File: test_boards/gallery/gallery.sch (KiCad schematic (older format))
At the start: 19 parts

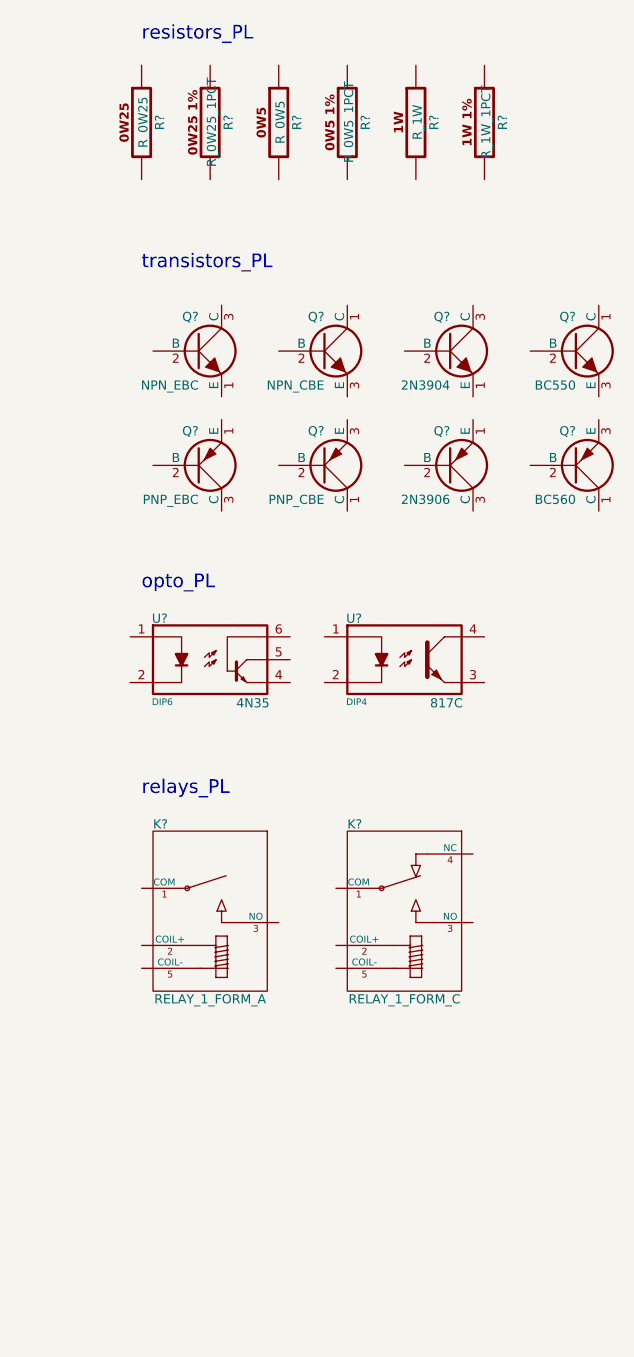
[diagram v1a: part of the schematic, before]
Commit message: tweaking relays, adding dc barrel jacks
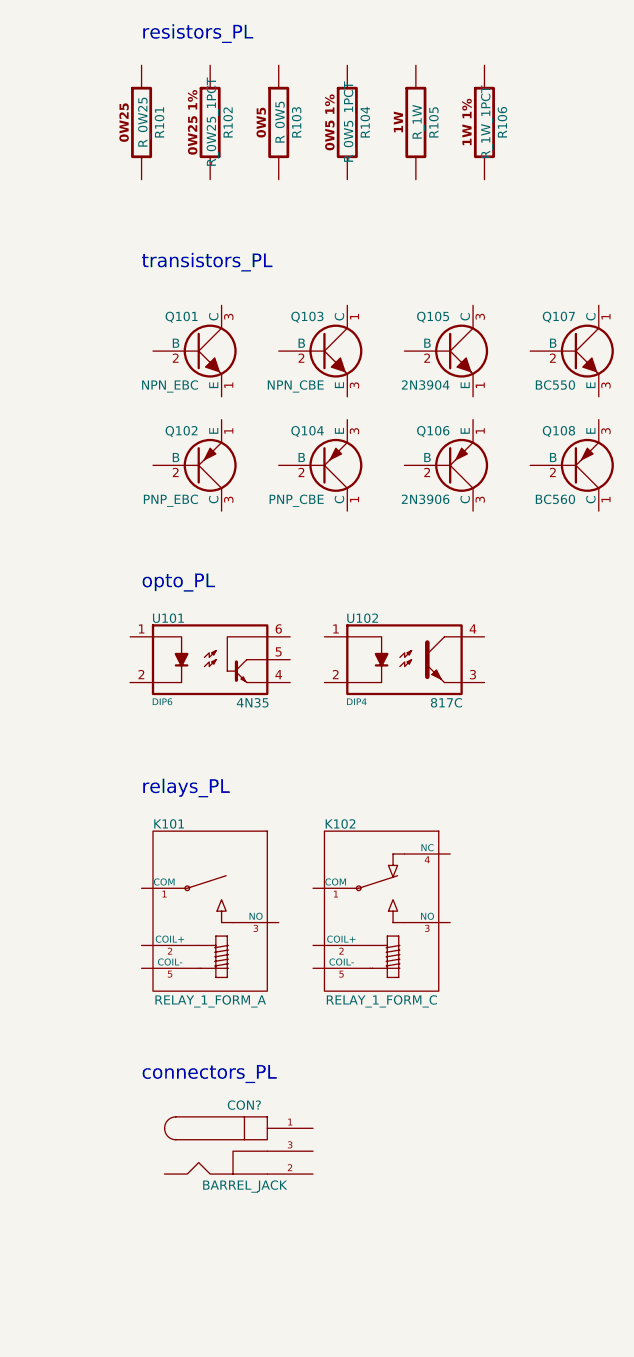
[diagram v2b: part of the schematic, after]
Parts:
- removed K?: RELAY_1_FORM_A, ~, symbol RELAY_1_FORM_A
- removed K?: RELAY_1_FORM_C, ~, symbol RELAY_1_FORM_C
- added CON?: BARREL_JACK, ~, symbol BARREL_JACK
- added K101: RELAY_1_FORM_A, ~, symbol RELAY_1_FORM_A
- added K102: RELAY_1_FORM_C, ~, symbol RELAY_1_FORM_C
- gave numbers to parts that had none: 17
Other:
- note added: "connectors_PL"
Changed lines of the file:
@@
 EESchema Schematic File Version 2
+LIBS:connectors_PL
 LIBS:transistors_PL
 LIBS:mounting_holes_PL
@@
 Sheet 1 1
 Title ""
-Date "15 mar 2014"
+Date "17 mar 2014"
 Rev ""
 Comp ""
@@
 $EndDescr
 $Comp
-L R_0W25 R?
+L R_0W25 R101
 U 1 1 5323CBE8
 P 700 1050
-F 0 "R?" V 780 1050 40  0000 C CNN
+F 0 "R101" V 780 1050 40  0000 C CNN
 F 1 "R_0W25" V 707 1051 40  0000 C CNN
 F 2 "~" V 630 1050 30  0000 C CNN
@@
 $EndComp
 $Comp
-L R_0W25_1PCT R?
+L R_0W25_1PCT R102
 U 1 1 5323CBF9
 P 1000 1050
-F 0 "R?" V 1080 1050 40  0000 C CNN
+F 0 "R102" V 1080 1050 40  0000 C CNN
 F 1 "R_0W25_1PCT" V 1007 1051 40  0000 C CNN
 F 2 "~" V 930 1050 30  0000 C CNN
@@
 $EndComp
 $Comp
-L R_0W5 R?
+L R_0W5 R103
 U 1 1 5323CC08
 P 1300 1050
-F 0 "R?" V 1380 1050 40  0000 C CNN
+F 0 "R103" V 1380 1050 40  0000 C CNN
 F 1 "R_0W5" V 1307 1051 40  0000 C CNN
 F 2 "~" V 1230 1050 30  0000 C CNN
@@
 $EndComp
 $Comp
-L R_0W5_1PCT R?
+L R_0W5_1PCT R104
 U 1 1 5323CC21
 P 1600 1050
-F 0 "R?" V 1680 1050 40  0000 C CNN
+F 0 "R104" V 1680 1050 40  0000 C CNN
 F 1 "R_0W5_1PCT" V 1607 1051 40  0000 C CNN
 F 2 "~" V 1530 1050 30  0000 C CNN
@@
 $EndComp
 $Comp
-L R_1W R?
+L R_1W R105
 U 1 1 5323CC30
 P 1900 1050
-F 0 "R?" V 1980 1050 40  0000 C CNN
+F 0 "R105" V 1980 1050 40  0000 C CNN
 F 1 "R_1W" V 1907 1051 40  0000 C CNN
 F 2 "~" V 1830 1050 30  0000 C CNN
@@
 $EndComp
 $Comp
-L R_1W_1PCT R?
+L R_1W_1PCT R106
 U 1 1 5323CC3F
 P 2200 1050
-F 0 "R?" V 2280 1050 40  0000 C CNN
+F 0 "R106" V 2280 1050 40  0000 C CNN
 F 1 "R_1W_1PCT" V 2207 1051 40  0000 C CNN
 F 2 "~" V 2130 1050 30  0000 C CNN
@@
 transistors_PL
 $Comp
-L 4N35 U?
+L 4N35 U101
 U 1 1 5323CCFD
 P 1000 3400
-F 0 "U?" H 745 3580 40  0000 L CNN
+F 0 "U101" H 745 3580 40  0000 L CNN
 F 1 "4N35" H 1260 3210 40  0000 R CNN
 F 2 "DIP6" H 745 3215 29  0000 L CNN
@@
 opto_PL
 $Comp
-L 817C U?
+L 817C U102
 U 1 1 5323CD26
 P 1850 3400
-F 0 "U?" H 1595 3580 40  0000 L CNN
+F 0 "U102" H 1595 3580 40  0000 L CNN
 F 1 "817C" H 2105 3210 40  0000 R CNN
 F 2 "DIP4" H 1595 3215 29  0000 L CNN
@@
 	1    0    0    -1
 $EndComp
-$Comp
-L RELAY_1_FORM_A K?
-U 1 1 5323CD50
-P 1000 4500
-F 0 "K?" H 750 4880 40  0000 L CNN
-F 1 "RELAY_1_FORM_A" H 1000 4115 40  0000 C CNN
-F 2 "~" H 995 4680 60  0000 C CNN
-F 3 "~" H 995 4680 60  0000 C CNN
-	1    1000 4500
-	1    0    0    -1
-$EndComp
-$Comp
-L RELAY_1_FORM_C K?
-U 1 1 5323CD5F
-P 1850 4500
-F 0 "K?" H 1600 4880 40  0000 L CNN
-F 1 "RELAY_1_FORM_C" H 1850 4115 40  0000 C CNN
-F 2 "~" H 1845 4680 60  0000 C CNN
-F 3 "~" H 1845 4680 60  0000 C CNN
-	1    1850 4500
-	1    0    0    -1
-$EndComp
 Text Notes 700  4000 0    60   ~ 0
 relays_PL
 $Comp
-L NPN_EBC Q?
+L NPN_EBC Q101
 U 1 1 5323DE26
 P 950 2050
-F 0 "Q?" H 950 2200 40  0000 R CNN
+F 0 "Q101" H 950 2200 40  0000 R CNN
 F 1 "NPN_EBC" H 950 1900 40  0000 R CNN
 F 2 "~" H 950 2050 60  0000 C CNN
@@
 $EndComp
 $Comp
-L PNP_EBC Q?
+L PNP_EBC Q102
 U 1 1 5323DE35
 P 950 2550
-F 0 "Q?" H 950 2700 40  0000 R CNN
+F 0 "Q102" H 950 2700 40  0000 R CNN
 F 1 "PNP_EBC" H 950 2400 40  0000 R CNN
 F 2 "~" H 950 2550 60  0000 C CNN
@@
 $EndComp
 $Comp
-L NPN_CBE Q?
+L NPN_CBE Q103
 U 1 1 5323DE44
 P 1500 2050
-F 0 "Q?" H 1500 2200 40  0000 R CNN
+F 0 "Q103" H 1500 2200 40  0000 R CNN
 F 1 "NPN_CBE" H 1500 1900 40  0000 R CNN
 F 2 "~" H 1500 2050 60  0000 C CNN
@@
 $EndComp
 $Comp
-L PNP_CBE Q?
+L PNP_CBE Q104
 U 1 1 5323DE53
 P 1500 2550
-F 0 "Q?" H 1500 2700 40  0000 R CNN
+F 0 "Q104" H 1500 2700 40  0000 R CNN
 F 1 "PNP_CBE" H 1500 2400 40  0000 R CNN
 F 2 "~" H 1500 2550 60  0000 C CNN
@@
 $EndComp
 $Comp
-L 2N3904 Q?
+L 2N3904 Q105
 U 1 1 5323DE62
 P 2050 2050
-F 0 "Q?" H 2050 2200 40  0000 R CNN
+F 0 "Q105" H 2050 2200 40  0000 R CNN
 F 1 "2N3904" H 2050 1900 40  0000 R CNN
 F 2 "~" H 2050 2050 60  0000 C CNN
@@
 $EndComp
 $Comp
-L 2N3906 Q?
+L 2N3906 Q106
 U 1 1 5323DE71
 P 2050 2550
-F 0 "Q?" H 2050 2700 40  0000 R CNN
+F 0 "Q106" H 2050 2700 40  0000 R CNN
 F 1 "2N3906" H 2050 2400 40  0000 R CNN
 F 2 "~" H 2050 2550 60  0000 C CNN
@@
 $EndComp
 $Comp
-L BC550 Q?
+L BC550 Q107
 U 1 1 5323DE80
 P 2600 2050
-F 0 "Q?" H 2600 2200 40  0000 R CNN
+F 0 "Q107" H 2600 2200 40  0000 R CNN
 F 1 "BC550" H 2600 1900 40  0000 R CNN
 F 2 "~" H 2600 2050 60  0000 C CNN
@@
 $EndComp
 $Comp
-L BC560 Q?
+L BC560 Q108
 U 1 1 5323DE8F
 P 2600 2550
-F 0 "Q?" H 2600 2700 40  0000 R CNN
+F 0 "Q108" H 2600 2700 40  0000 R CNN
 F 1 "BC560" H 2600 2400 40  0000 R CNN
 F 2 "~" H 2600 2550 60  0000 C CNN
@@
 $EndComp
 $Comp
-L HOLE H?
+L HOLE H101
 U 1 1 5323DFF1
 P 750 7550
-F 0 "H?" H 750 7605 40  0000 C CNN
+F 0 "H101" H 750 7605 40  0000 C CNN
 F 1 "HOLE" H 750 7490 30  0000 C CNN
 F 2 "~" H 750 7550 60  0000 C CNN
@@
 Text Notes 700  7350 0    60   ~ 0
 mounting_holes_PL
+Text Notes 700  5250 0    60   ~ 0
+connectors_PL
+$Comp
+L RELAY_1_FORM_A K101
+U 1 1 53265C18
+P 1000 4500
+F 0 "K101" H 750 4880 40  0000 L CNN
+F 1 "RELAY_1_FORM_A" H 1000 4110 40  0000 C CNN
+F 2 "~" H 995 4680 60  0000 C CNN
+F 3 "~" H 995 4680 60  0000 C CNN
+	1    1000 4500
+	1    0    0    -1
+$EndComp
+$Comp
+L RELAY_1_FORM_C K102
+U 1 1 53265C27
+P 1750 4500
+F 0 "K102" H 1500 4880 40  0000 L CNN
+F 1 "RELAY_1_FORM_C" H 1750 4110 40  0000 C CNN
+F 2 "~" H 1745 4680 60  0000 C CNN
+F 3 "~" H 1745 4680 60  0000 C CNN
+	1    1750 4500
+	1    0    0    -1
+$EndComp
+$Comp
+L BARREL_JACK CON?
+U 1 1 53265E33
+P 1150 5550
+F 0 "CON?" H 1150 5750 40  0000 C CNN
+F 1 "BARREL_JACK" H 1150 5400 40  0000 C CNN
+F 2 "~" H 1150 5550 60  0000 C CNN
+F 3 "~" H 1150 5550 60  0000 C CNN
+	1    1150 5550
+	1    0    0    -1
+$EndComp
 $EndSCHEMATC

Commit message: adding regulators and displays
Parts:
- added DS?: AMMETER_H, ~, symbol AMMETER_H
- added DS?: AMMETER_V, ~, symbol AMMETER_V
- added DS?: VOLTMETER, ~, symbol VOLTMETER
- added U?: 7805, ~, symbol 7805
- added U?: 78L05, ~, symbol 78L05
- added U?: LM317, ~, symbol LM317
- added U?: LM337, ~, symbol LM337
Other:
- note added: "displays_PL"
- note added: "regulators_PL"
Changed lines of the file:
@@
 EESchema Schematic File Version 2
+LIBS:displays_PL
+LIBS:regulators_PL
 LIBS:connectors_PL
 LIBS:transistors_PL
@@
 Sheet 1 1
 Title ""
-Date "17 mar 2014"
+Date "20 mar 2014"
 Rev ""
 Comp ""
@@
 	1    0    0    -1
 $EndComp
+$Comp
+L AMMETER_H DS?
+U 1 1 532A694E
+P 1700 5500
+F 0 "DS?" H 1750 5650 40  0000 L CNN
+F 1 "AMMETER_H" H 2550 5100 40  0000 R CNN
+F 2 "~" H 2530 5900 60  0000 C CNN
+F 3 "~" H 2530 5900 60  0000 C CNN
+	1    1700 5500
+	1    0    0    -1
+$EndComp
+$Comp
+L AMMETER_V DS?
+U 1 1 532A695D
+P 2850 5500
+F 0 "DS?" H 2900 5650 40  0000 L CNN
+F 1 "AMMETER_V" H 3700 5100 40  0000 R CNN
+F 2 "~" H 3680 5900 60  0000 C CNN
+F 3 "~" H 3680 5900 60  0000 C CNN
+	1    2850 5500
+	1    0    0    -1
+$EndComp
+$Comp
+L VOLTMETER DS?
+U 1 1 532A696C
+P 4000 5500
+F 0 "DS?" H 4050 5650 40  0000 L CNN
+F 1 "VOLTMETER" H 4850 5100 40  0000 R CNN
+F 2 "~" H 4830 5900 60  0000 C CNN
+F 3 "~" H 4830 5900 60  0000 C CNN
+	1    4000 5500
+	1    0    0    -1
+$EndComp
+Text Notes 1650 5250 0    60   ~ 0
+displays_PL
+$Comp
+L 7805 U?
+U 1 1 532A6997
+P 1050 6500
+F 0 "U?" H 850 6660 40  0000 L BNN
+F 1 "7805" H 1250 6330 40  0000 R TNN
+F 2 "~" H 1050 6500 60  0000 C CNN
+F 3 "~" H 1050 6500 60  0000 C CNN
+	1    1050 6500
+	1    0    0    -1
+$EndComp
+$Comp
+L 78L05 U?
+U 1 1 532A69B5
+P 1800 6500
+F 0 "U?" H 1600 6660 40  0000 L BNN
+F 1 "78L05" H 2000 6330 40  0000 R TNN
+F 2 "~" H 1800 6500 60  0000 C CNN
+F 3 "~" H 1800 6500 60  0000 C CNN
+	1    1800 6500
+	1    0    0    -1
+$EndComp
+$Comp
+L LM317 U?
+U 1 1 532A69C4
+P 2550 6500
+F 0 "U?" H 2350 6660 40  0000 L BNN
+F 1 "LM317" H 2750 6330 40  0000 R TNN
+F 2 "~" H 2550 6500 60  0000 C CNN
+F 3 "~" H 2550 6500 60  0000 C CNN
+	1    2550 6500
+	1    0    0    -1
+$EndComp
+$Comp
+L LM337 U?
+U 1 1 532A69D3
+P 3300 6500
+F 0 "U?" H 3100 6660 40  0000 L BNN
+F 1 "LM337" H 3500 6330 40  0000 R TNN
+F 2 "~" H 3300 6500 60  0000 C CNN
+F 3 "~" H 3300 6500 60  0000 C CNN
+	1    3300 6500
+	1    0    0    -1
+$EndComp
+Text Notes 750  6250 0    60   ~ 0
+regulators_PL
 $EndSCHEMATC

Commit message: updating gallery schematic
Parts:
- added C?: C_CER, ~, symbol C_CER
- added C?: C_EL, ~, symbol C_EL
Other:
- note added: "capacitors_PL"
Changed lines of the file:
@@
 EESchema Schematic File Version 2
+LIBS:capacitors_PL
 LIBS:displays_PL
 LIBS:regulators_PL
@@
 Sheet 1 1
 Title ""
-Date "20 mar 2014"
+Date "23 mar 2014"
 Rev ""
 Comp ""
@@
 Text Notes 750  6250 0    60   ~ 0
 regulators_PL
+Text Notes 2900 700  0    60   ~ 0
+capacitors_PL
+$Comp
+L C_CER C?
+U 1 1 532F0423
+P 3000 1000
+F 0 "C?" H 3020 1060 30  0000 L BNN
+F 1 "C_CER" H 3020 940 30  0000 L TNN
+F 2 "~" H 3038 850 30  0000 C CNN
+F 3 "~" H 3000 1000 60  0000 C CNN
+	1    3000 1000
+	1    0    0    -1
+$EndComp
+$Comp
+L C_EL C?
+U 1 1 532F0432
+P 3350 1000
+F 0 "C?" H 3370 1060 30  0000 L BNN
+F 1 "C_EL" H 3370 910 30  0000 L TNN
+F 2 "~" H 3388 850 30  0000 C CNN
+F 3 "~" H 3350 1000 60  0000 C CNN
+	1    3350 1000
+	1    0    0    -1
+$EndComp
 $EndSCHEMATC

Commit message: tweaking caps
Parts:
- gave numbers to parts that had none: 10
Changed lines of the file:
@@
 $EndComp
 $Comp
-L BARREL_JACK CON?
+L BARREL_JACK CON101
 U 1 1 53265E33
 P 1150 5550
-F 0 "CON?" H 1150 5750 40  0000 C CNN
+F 0 "CON101" H 1150 5750 40  0000 C CNN
 F 1 "BARREL_JACK" H 1150 5400 40  0000 C CNN
 F 2 "~" H 1150 5550 60  0000 C CNN
@@
 $EndComp
 $Comp
-L AMMETER_H DS?
+L AMMETER_H DS101
 U 1 1 532A694E
 P 1700 5500
-F 0 "DS?" H 1750 5650 40  0000 L CNN
+F 0 "DS101" H 1750 5650 40  0000 L CNN
 F 1 "AMMETER_H" H 2550 5100 40  0000 R CNN
 F 2 "~" H 2530 5900 60  0000 C CNN
@@
 $EndComp
 $Comp
-L AMMETER_V DS?
+L AMMETER_V DS102
 U 1 1 532A695D
 P 2850 5500
-F 0 "DS?" H 2900 5650 40  0000 L CNN
+F 0 "DS102" H 2900 5650 40  0000 L CNN
 F 1 "AMMETER_V" H 3700 5100 40  0000 R CNN
 F 2 "~" H 3680 5900 60  0000 C CNN
@@
 $EndComp
 $Comp
-L VOLTMETER DS?
+L VOLTMETER DS103
 U 1 1 532A696C
 P 4000 5500
-F 0 "DS?" H 4050 5650 40  0000 L CNN
+F 0 "DS103" H 4050 5650 40  0000 L CNN
 F 1 "VOLTMETER" H 4850 5100 40  0000 R CNN
 F 2 "~" H 4830 5900 60  0000 C CNN
@@
 displays_PL
 $Comp
-L 7805 U?
+L 7805 U103
 U 1 1 532A6997
 P 1050 6500
-F 0 "U?" H 850 6660 40  0000 L BNN
+F 0 "U103" H 850 6660 40  0000 L BNN
 F 1 "7805" H 1250 6330 40  0000 R TNN
 F 2 "~" H 1050 6500 60  0000 C CNN
@@
 $EndComp
 $Comp
-L 78L05 U?
+L 78L05 U104
 U 1 1 532A69B5
 P 1800 6500
-F 0 "U?" H 1600 6660 40  0000 L BNN
+F 0 "U104" H 1600 6660 40  0000 L BNN
 F 1 "78L05" H 2000 6330 40  0000 R TNN
 F 2 "~" H 1800 6500 60  0000 C CNN
@@
 $EndComp
 $Comp
-L LM317 U?
+L LM317 U105
 U 1 1 532A69C4
 P 2550 6500
-F 0 "U?" H 2350 6660 40  0000 L BNN
+F 0 "U105" H 2350 6660 40  0000 L BNN
 F 1 "LM317" H 2750 6330 40  0000 R TNN
 F 2 "~" H 2550 6500 60  0000 C CNN
@@
 $EndComp
 $Comp
-L LM337 U?
+L LM337 U106
 U 1 1 532A69D3
 P 3300 6500
-F 0 "U?" H 3100 6660 40  0000 L BNN
+F 0 "U106" H 3100 6660 40  0000 L BNN
 F 1 "LM337" H 3500 6330 40  0000 R TNN
 F 2 "~" H 3300 6500 60  0000 C CNN
@@
 capacitors_PL
 $Comp
-L C_CER C?
+L C_CER C101
 U 1 1 532F0423
 P 3000 1000
-F 0 "C?" H 3020 1060 30  0000 L BNN
+F 0 "C101" H 3020 1060 30  0000 L BNN
 F 1 "C_CER" H 3020 940 30  0000 L TNN
 F 2 "~" H 3038 850 30  0000 C CNN
@@
 $EndComp
 $Comp
-L C_EL C?
+L C_EL C102
 U 1 1 532F0432
 P 3350 1000
-F 0 "C?" H 3370 1060 30  0000 L BNN
+F 0 "C102" H 3370 1060 30  0000 L BNN
 F 1 "C_EL" H 3370 910 30  0000 L TNN
 F 2 "~" H 3388 850 30  0000 C CNN

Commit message: adding mini toggle switch
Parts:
- added SW?: SPDT, ~, symbol SPDT
- added SW?: SP6T, ~, symbol SP6T
- added SW?: DP6T, ~, symbol DP6T
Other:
- note added: "switches_PL"
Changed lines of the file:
@@
 EESchema Schematic File Version 2
+LIBS:switches_PL
 LIBS:capacitors_PL
 LIBS:displays_PL
@@
 	1    0    0    -1
 $EndComp
+$Comp
+L SPDT SW?
+U 1 1 532F106F
+P 2500 4300
+F 0 "SW?" H 2720 4400 40  0000 C CNN
+F 1 "SPDT" H 2780 4230 40  0000 C CNN
+F 2 "~" H 2880 4300 60  0000 C CNN
+F 3 "~" H 2880 4300 60  0000 C CNN
+	1    2500 4300
+	1    0    0    -1
+$EndComp
+Text Notes 2450 4000 0    60   ~ 0
+switches_PL
+$Comp
+L SP6T SW?
+U 1 1 532F108A
+P 3600 4500
+F 0 "SW?" H 3900 4550 40  0000 C CNN
+F 1 "SP6T" H 3900 4450 40  0000 C CNN
+F 2 "~" H 3600 5500 60  0000 C CNN
+F 3 "~" H 3600 5500 60  0000 C CNN
+	1    3600 4500
+	1    0    0    -1
+$EndComp
+$Comp
+L DP6T SW?
+U 1 1 532F1099
+P 5400 4500
+F 0 "SW?" H 5700 4550 40  0000 C CNN
+F 1 "DP6T" H 5700 4450 40  0000 C CNN
+F 2 "~" H 5400 5500 60  0000 C CNN
+F 3 "~" H 5400 5500 60  0000 C CNN
+	1    5400 4500
+	1    0    0    -1
+$EndComp

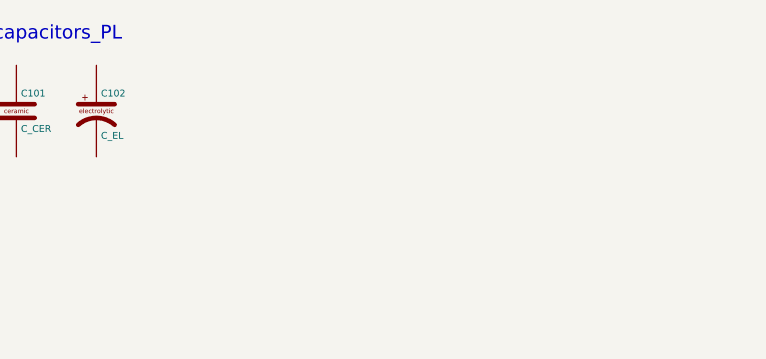
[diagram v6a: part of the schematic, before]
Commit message: adding diodes
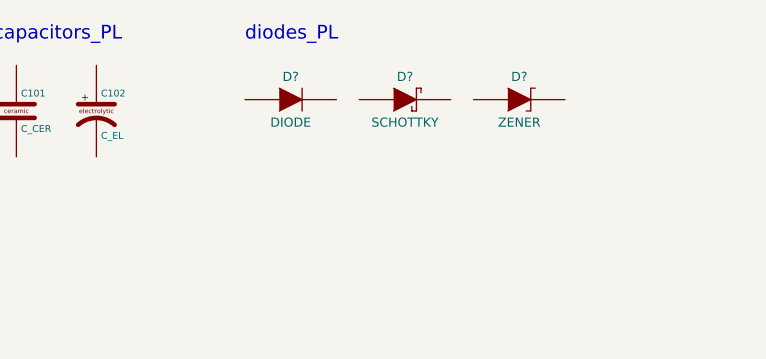
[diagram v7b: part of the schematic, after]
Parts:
- added D?: DIODE, ~, symbol DIODE
- added D?: SCHOTTKY, ~, symbol SCHOTTKY
- added D?: ZENER, ~, symbol ZENER
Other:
- note added: "diodes_PL"
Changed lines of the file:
@@
 EESchema Schematic File Version 2
+LIBS:diodes_PL
 LIBS:switches_PL
 LIBS:capacitors_PL
@@
 	1    0    0    -1
 $EndComp
+Text Notes 4000 700  0    60   ~ 0
+diodes_PL
+$Comp
+L DIODE D?
+U 1 1 532F4AEC
+P 4200 950
+F 0 "D?" H 4200 1050 40  0000 C CNN
+F 1 "DIODE" H 4200 850 40  0000 C CNN
+F 2 "~" H 4200 950 60  0000 C CNN
+F 3 "~" H 4200 950 60  0000 C CNN
+	1    4200 950
+	1    0    0    -1
+$EndComp
+$Comp
+L SCHOTTKY D?
+U 1 1 532F4AFB
+P 4700 950
+F 0 "D?" H 4700 1050 40  0000 C CNN
+F 1 "SCHOTTKY" H 4700 850 40  0000 C CNN
+F 2 "~" H 4700 950 60  0000 C CNN
+F 3 "~" H 4700 950 60  0000 C CNN
+	1    4700 950
+	1    0    0    -1
+$EndComp
+$Comp
+L ZENER D?
+U 1 1 532F4B0A
+P 5200 950
+F 0 "D?" H 5200 1050 40  0000 C CNN
+F 1 "ZENER" H 5200 850 40  0000 C CNN
+F 2 "~" H 5200 950 60  0000 C CNN
+F 3 "~" H 5200 950 60  0000 C CNN
+	1    5200 950
+	1    0    0    -1
+$EndComp

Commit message: adding potentiometer symbols
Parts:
- added RV?: POT, ~, symbol POT
- added RV?: POT_10T, ~, symbol POT_10T
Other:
- moved on the sheet: C101, C102, D?
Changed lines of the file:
@@
 Text Notes 750  6250 0    60   ~ 0
 regulators_PL
-Text Notes 2900 700  0    60   ~ 0
+Text Notes 3850 700  0    60   ~ 0
 capacitors_PL
 $Comp
 L C_CER C101
 U 1 1 532F0423
-P 3000 1000
-F 0 "C101" H 3020 1060 30  0000 L BNN
-F 1 "C_CER" H 3020 940 30  0000 L TNN
-F 2 "~" H 3038 850 30  0000 C CNN
-F 3 "~" H 3000 1000 60  0000 C CNN
-	1    3000 1000
+P 3950 1000
+F 0 "C101" H 3970 1060 30  0000 L BNN
+F 1 "C_CER" H 3970 940 30  0000 L TNN
+F 2 "~" H 3988 850 30  0000 C CNN
+F 3 "~" H 3950 1000 60  0000 C CNN
+	1    3950 1000
 	1    0    0    -1
 $EndComp
@@
 L C_EL C102
 U 1 1 532F0432
-P 3350 1000
-F 0 "C102" H 3370 1060 30  0000 L BNN
-F 1 "C_EL" H 3370 910 30  0000 L TNN
-F 2 "~" H 3388 850 30  0000 C CNN
-F 3 "~" H 3350 1000 60  0000 C CNN
-	1    3350 1000
+P 4300 1000
+F 0 "C102" H 4320 1060 30  0000 L BNN
+F 1 "C_EL" H 4320 910 30  0000 L TNN
+F 2 "~" H 4338 850 30  0000 C CNN
+F 3 "~" H 4300 1000 60  0000 C CNN
+	1    4300 1000
 	1    0    0    -1
 $EndComp
@@
 	1    0    0    -1
 $EndComp
-Text Notes 4000 700  0    60   ~ 0
+Text Notes 4950 700  0    60   ~ 0
 diodes_PL
 $Comp
 L DIODE D?
 U 1 1 532F4AEC
-P 4200 950
-F 0 "D?" H 4200 1050 40  0000 C CNN
-F 1 "DIODE" H 4200 850 40  0000 C CNN
-F 2 "~" H 4200 950 60  0000 C CNN
-F 3 "~" H 4200 950 60  0000 C CNN
-	1    4200 950
+P 5150 950
+F 0 "D?" H 5150 1050 40  0000 C CNN
+F 1 "DIODE" H 5150 850 40  0000 C CNN
+F 2 "~" H 5150 950 60  0000 C CNN
+F 3 "~" H 5150 950 60  0000 C CNN
+	1    5150 950
 	1    0    0    -1
 $EndComp
@@
 L SCHOTTKY D?
 U 1 1 532F4AFB
-P 4700 950
-F 0 "D?" H 4700 1050 40  0000 C CNN
-F 1 "SCHOTTKY" H 4700 850 40  0000 C CNN
-F 2 "~" H 4700 950 60  0000 C CNN
-F 3 "~" H 4700 950 60  0000 C CNN
-	1    4700 950
+P 5650 950
+F 0 "D?" H 5650 1050 40  0000 C CNN
+F 1 "SCHOTTKY" H 5650 850 40  0000 C CNN
+F 2 "~" H 5650 950 60  0000 C CNN
+F 3 "~" H 5650 950 60  0000 C CNN
+	1    5650 950
 	1    0    0    -1
 $EndComp
@@
 L ZENER D?
 U 1 1 532F4B0A
-P 5200 950
-F 0 "D?" H 5200 1050 40  0000 C CNN
-F 1 "ZENER" H 5200 850 40  0000 C CNN
-F 2 "~" H 5200 950 60  0000 C CNN
-F 3 "~" H 5200 950 60  0000 C CNN
-	1    5200 950
+P 6150 950
+F 0 "D?" H 6150 1050 40  0000 C CNN
+F 1 "ZENER" H 6150 850 40  0000 C CNN
+F 2 "~" H 6150 950 60  0000 C CNN
+F 3 "~" H 6150 950 60  0000 C CNN
+	1    6150 950
 	1    0    0    -1
 $EndComp
+$Comp
+L POT RV?
+U 1 1 532F5FE3
+P 2700 1050
+F 0 "RV?" H 2525 1135 30  0000 C CNN
+F 1 "POT" H 2895 1010 30  0000 C CNN
+F 2 "~" H 2700 1050 60  0000 C CNN
+F 3 "~" H 2700 1050 60  0000 C CNN
+	1    2700 1050
+	1    0    0    -1
+$EndComp
+$Comp
+L POT_10T RV?
+U 1 1 532F5FF2
+P 3350 1050
+F 0 "RV?" H 3175 1135 30  0000 C CNN
+F 1 "POT_10T" H 3545 1010 30  0000 C CNN
+F 2 "~" H 3350 1050 60  0000 C CNN
+F 3 "~" H 3350 1050 60  0000 C CNN
+	1    3350 1050
+	1    0    0    -1
+$EndComp
